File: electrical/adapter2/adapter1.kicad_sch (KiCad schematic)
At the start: 7 parts, among them J2 Conn_01x08_Pin

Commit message: start working on adapter2 PCB
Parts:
- added C1, C10, C11, C12, C2, C5, C7, C8, C9: 105, Capacitor_SMD:C_0805_2012Metric_Pad1.18x1.45mm_HandSolder, symbol Device:C
- added C15, C3: 104 !, Capacitor_SMD:C_0805_2012Metric_Pad1.18x1.45mm_HandSolder, symbol Device:C
- added C4, C6: 4.7uF/50V, Capacitor_SMD:C_0805_2012Metric_Pad1.18x1.45mm_HandSolder, symbol Device:C
- added D1, D2, D3: MBR0530, Diode_SMD:D_SOD-123, symbol Diode:MBR0530
- added J3, J4: 0.5 mm, 24P, Connector_FFC-FPC:Jushuo_AFC07-S24FCA-00_1x24-1MP_P0.50_Horizontal, symbol Connector_Generic_MountingPin:Conn_01x24_MountingPin
- added JP3: SolderJumper_3_Bridged12, Jumper:SolderJumper-3_P1.3mm_Bridged12_RoundedPad1.0x1.5mm, symbol Jumper:SolderJumper_3_Bridged12
- added JP4: SolderJumper_2_Open, Jumper:SolderJumper-2_P1.3mm_Open_TrianglePad1.0x1.5mm, symbol Jumper:SolderJumper_2_Open
- added L1: 68uH, symbol Device:L
- added Q1: BSS138, Package_TO_SOT_SMD:SOT-23, symbol Transistor_FET:BSS138
- added Q2: AO3401A, Package_TO_SOT_SMD:SOT-23, symbol Transistor_FET:AO3401A
- added Q3: S8050 SMD, Package_TO_SOT_SMD:SOT-23, symbol Transistor_BJT:BC817
- added R1: 0.47R, Resistor_SMD:R_0805_2012Metric_Pad1.20x1.40mm_HandSolder, symbol Device:R
- added R2, R5: 10k, Resistor_SMD:R_0805_2012Metric_Pad1.20x1.40mm_HandSolder, symbol Device:R
- added R3: 100k, Resistor_SMD:R_0805_2012Metric_Pad1.20x1.40mm_HandSolder, symbol Device:R
- added R6: 1k, Resistor_SMD:R_0805_2012Metric_Pad1.20x1.40mm_HandSolder, symbol Device:R
- added R7, R8: 47k, Resistor_SMD:R_0805_2012Metric_Pad1.20x1.40mm_HandSolder, symbol Device:R
- added U1: ~, fw16_epaper:RP2040-Tiny, symbol fw16_epaper:RP2040-Tiny
- renumbered R1 to R10
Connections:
- net +3V3: now also C15.2, C4.2, JP4.1 (A), L1.1, Q2.2 (S), R3.2
- net GND: now also C1.1, C10.1, C11.1, C12.1, C15.1, C2.1, C3.1, C4.1, C5.1, C7.1, C8.1, C9.1, D1.1 (K), J3.8 (Pin_8), J3.MP (MountPin), J4.17 (Pin_17), JP3.1 (A), Q3.2 (E), R1.1, R2.1, R7.1, R8.1, U1.21 (GND)
- net SLEEP: now also U1.0
- new net: Q3.1 (B), R5.1, R7.2
- new net: C12.2, J3.1 (Pin_1), J4.24 (Pin_24)
- new net: J3.18 (Pin_18), J4.7 (Pin_7)
- new net: J3.19 (Pin_19), J4.6 (Pin_6)
- new net: C2.2, J3.20 (Pin_20), J4.5 (Pin_5)
- new net: C1.2, J3.21 (Pin_21), J4.4 (Pin_4)
- new net: J3.24 (Pin_24), J4.1 (Pin_1)
- new net: C10.2, J3.3 (Pin_3), J4.22 (Pin_22)
- new net: C8.2, J3.5 (Pin_5), J4.20 (Pin_20)
- new net: C7.2, J3.6 (Pin_6), J4.19 (Pin_19)
- new net: C5.2, J3.7 (Pin_7), J4.18 (Pin_18)
- new net: C6.2, D3.2 (A), L1.2, Q1.3 (D)
- new net: Q1.1 (G), R2.2
- new net: Q2.1 (G), Q3.3 (C), R3.1
- new net: Q1.2 (S), R1.2
- new net: C6.1, D1.2 (A), D2.1 (K)
- new net 3V3_EP: C3.2, J3.10 (Pin_10), J3.9 (Pin_9), J4.15 (Pin_15), J4.16 (Pin_16), JP3.3 (B), Q2.3 (D)
- new net 3V3_RPI: JP4.2 (B), U1.20 (3V3)
- new net 5V_RPI: U1.22 (5V)
- new net BS: J3.17 (Pin_17), J4.8 (Pin_8), JP3.2 (C)
- new net BUSY: J3.16 (Pin_16), J4.9 (Pin_9), U1.14
- new net CS: J3.13 (Pin_13), J4.12 (Pin_12), U1.19 (29)
- new net DC: J3.14 (Pin_14), J4.11 (Pin_11), U1.18 (28)
- new net DIN: J3.11 (Pin_11), J4.14 (Pin_14), U1.17 (27)
- new net GDR: J3.23 (Pin_23), J4.2 (Pin_2)
- new net PREVGH: C9.2, D3.1 (K), J3.4 (Pin_4), J4.21 (Pin_21)
- new net PREVGL: C11.2, D2.2 (A), J3.2 (Pin_2), J4.23 (Pin_23)
- new net RESE: J3.22 (Pin_22), J4.3 (Pin_3)
- new net RST: J3.15 (Pin_15), J4.10 (Pin_10), R5.2, R6.1, U1.15
- new net SCK: J3.12 (Pin_12), J4.13 (Pin_13), U1.16 (26)
- new net VCC_EN: R6.2, R8.2
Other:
- note added: "ADC"
- note added: "This is a mirrored connector on top. It could be used to solder the FPC directly (without socket) but that's probably not a good idea ;-)"
- note added: "This is pin 1. Connector is flipped in KiCad."
- note added: "see https://files.waveshare.com/upload/1/1c/Pico-ePaper-3.7.pdf"

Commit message: adapter2: routing done and DRC clean
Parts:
- removed R6: 1k, Resistor_SMD:R_0805_2012Metric_Pad1.20x1.40mm_HandSolder, symbol Device:R
- removed R8: 47k, Resistor_SMD:R_0805_2012Metric_Pad1.20x1.40mm_HandSolder, symbol Device:R
- added J5: ~, fw16_epaper:TouchConnector, symbol Connector:Conn_01x04_Socket
- L1: footprint (none) -> Inductor_SMD:L_Bourns-SRN4018
- R10: footprint Resistor_SMD:R_0603_1608Metric_Pad0.98x0.95mm_HandSolder -> Resistor_SMD:R_0805_2012Metric_Pad1.20x1.40mm_HandSolder
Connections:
- net +3V3: no longer C4.2, L1.1
- net 3V3_EP: now also C4.2, L1.1
- net BUSY: now also U1.5; no longer U1.14
- net CS: now also U1.8; no longer U1.19 (29)
- net DC: now also U1.7; no longer U1.18 (28)
- net DIN: now also U1.10; no longer U1.17 (27)
- net GDR: now also Q1.1 (G), R2.2
- net GND: now also J4.MP (MountPin)
- net RESE: now also Q1.2 (S), R1.2
- net RST: now also U1.6; no longer U1.15
- net SCK: now also U1.9; no longer U1.16 (26)
- net at U1.1: now also U1.19 (29), J5.1 (Pin_1)
- net at U1.2: now also U1.18 (28), J5.2 (Pin_2)
- net at U1.3: now also U1.17 (27), J5.3 (Pin_3)
- net at U1.4: now also U1.16 (26), J5.4 (Pin_4)
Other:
- note added: "Touch"

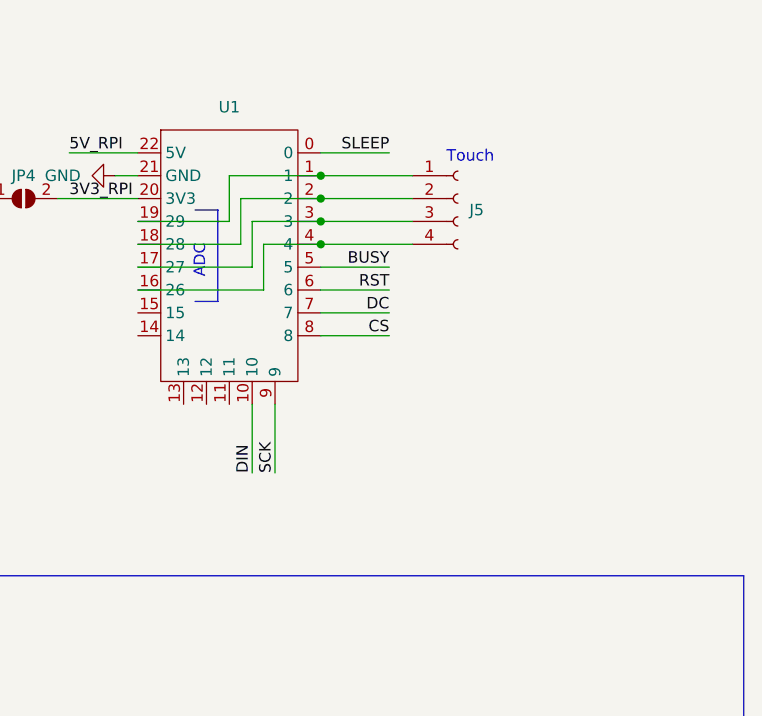
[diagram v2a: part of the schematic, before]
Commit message: add ATECC608
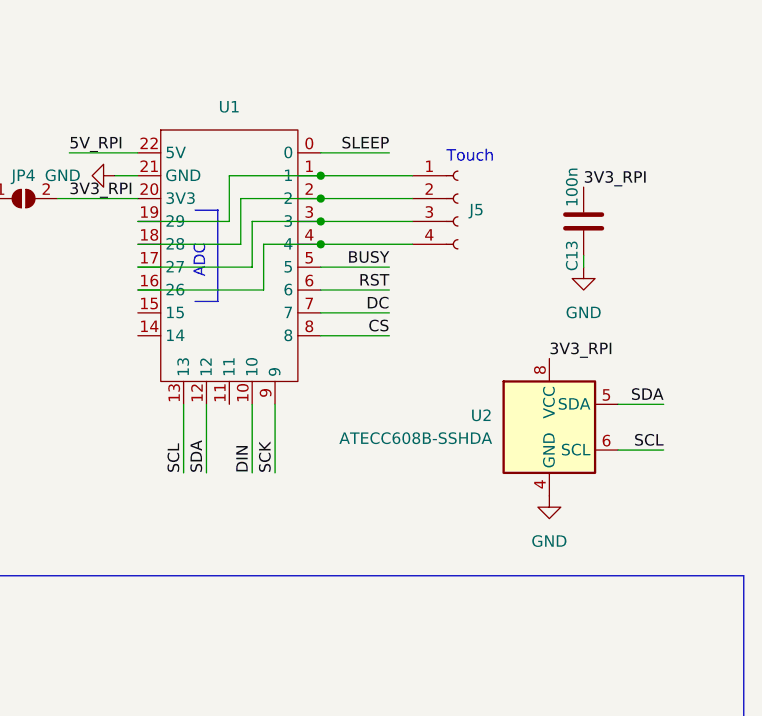
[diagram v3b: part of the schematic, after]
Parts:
- added C13: 100n, Capacitor_SMD:C_0805_2012Metric_Pad1.18x1.45mm_HandSolder, symbol Device:C
- added U2: ATECC608B-SSHDA, Package_SO:SOIC-8_3.9x4.9mm_P1.27mm, symbol Security:ATECC608B-SSHDA
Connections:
- net 3V3_RPI: now also C13.2, U2.8 (VCC)
- net GND: now also C13.1, U2.4 (GND)
- net SDA: now reaches U1.12
- net SDA: now also U2.5 (SDA)
- net SCL: now reaches U1.13
- net SCL: now also U2.6 (SCL)
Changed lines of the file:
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@@
+    (stroke (width 0) (type default))
+  )
+  (wire (pts (xy 173.99 59.69) (xy 179.07 59.69))
     (stroke (width 0) (type default))
   )
@@
     (stroke (width 0) (type default))
   )
+  (wire (pts (xy 128.27 59.69) (xy 128.27 67.31))
+    (stroke (width 0) (type default))
+  )
+  (wire (pts (xy 170.18 44.45) (xy 170.18 43.18))
+    (stroke (width 0) (type default))
+  )
   (wire (pts (xy 22.86 40.64) (xy 30.48 40.64))
     (stroke (width 0) (type default))
@@
     (stroke (width 0) (type default))
   )
+  (wire (pts (xy 173.99 64.77) (xy 179.07 64.77))
+    (stroke (width 0) (type default))
+  )
   (wire (pts (xy 148.59 49.53) (xy 140.97 49.53))
     (stroke (width 0) (type default))
@@
   )
   (wire (pts (xy 53.34 40.64) (xy 60.96 40.64))
+    (stroke (width 0) (type default))
+  )
+  (wire (pts (xy 125.73 59.69) (xy 125.73 67.31))
     (stroke (width 0) (type default))
   )
@@
     (effects (font (size 1.27 1.27)) (justify left bottom))
   )
+  (label "3V3_RPI" (at 170.18 35.56 0) (fields_autoplaced)
+    (effects (font (size 1.27 1.27)) (justify left bottom))
+  )
   (label "GDR" (at 44.45 97.79 0) (fields_autoplaced)
+    (effects (font (size 1.27 1.27)) (justify left bottom))
+  )
+  (label "SCL" (at 125.73 67.31 90) (fields_autoplaced)
     (effects (font (size 1.27 1.27)) (justify left bottom))
   )
@@
     (effects (font (size 1.27 1.27)) (justify left bottom))
   )
+  (label "3V3_RPI" (at 166.37 54.61 0) (fields_autoplaced)
+    (effects (font (size 1.27 1.27)) (justify left bottom))
+  )
   (label "RST" (at 44.45 118.11 0) (fields_autoplaced)
     (effects (font (size 1.27 1.27)) (justify left bottom))
@@
   (label "BS" (at 44.45 113.03 0) (fields_autoplaced)
     (effects (font (size 1.27 1.27)) (justify left bottom))
+  )
+  (label "SCL" (at 179.07 64.77 180) (fields_autoplaced)
+    (effects (font (size 1.27 1.27)) (justify right bottom))
   )
   (label "RESE" (at 44.45 100.33 0) (fields_autoplaced)
@@
     (effects (font (size 1.27 1.27)) (justify right bottom))
   )
+  (label "SDA" (at 128.27 67.31 90) (fields_autoplaced)
+    (effects (font (size 1.27 1.27)) (justify left bottom))
+  )
   (label "RUN" (at 62.23 54.61 0) (fields_autoplaced)
     (effects (font (size 1.27 1.27)) (justify left bottom))
@@
   (label "RUN" (at 38.1 64.77 90) (fields_autoplaced)
     (effects (font (size 1.27 1.27)) (justify left bottom))
+  )
+  (label "SDA" (at 179.07 59.69 180) (fields_autoplaced)
+    (effects (font (size 1.27 1.27)) (justify right bottom))
   )
   (label "PREVGL" (at 111.76 191.77 0) (fields_autoplaced)
@@
         (path "/a61be344-1595-4e77-a084-104edbf00aaf"
           (reference "#PWR014") (unit 1)
+        )
+      )
+    )
+  )
+  (symbol (lib_id "power:GND") (at 166.37 69.85 0) (unit 1)
+    (in_bom yes) (on_board yes) (dnp no) (fields_autoplaced)
+    (property "Reference" "#PWR036" (at 166.37 76.2 0)
+      (effects (font (size 1.27 1.27)) hide)
+    )
+    (property "Value" "GND" (at 166.37 74.93 0)
+      (effects (font (size 1.27 1.27)))
+    )
+    (property "Footprint" "" (at 166.37 69.85 0)
+      (effects (font (size 1.27 1.27)) hide)
+    )
+    (property "Datasheet" "" (at 166.37 69.85 0)
+      (effects (font (size 1.27 1.27)) hide)
+    )
+    (pin "1")
+    (instances
+      (project "adapter1"
+        (path "/a61be344-1595-4e77-a084-104edbf00aaf"
+          (reference "#PWR036") (unit 1)
         )
       )
@@
     )
   )
+  (symbol (lib_id "Device:C") (at 170.18 39.37 180) (unit 1)
+    (in_bom yes) (on_board yes) (dnp no)
+    (property "Reference" "C13" (at 168.91 43.18 90)
+      (effects (font (size 1.27 1.27)))
+    )
+    (property "Value" "100n" (at 168.91 35.56 90)
+      (effects (font (size 1.27 1.27)))
+    )
+    (property "Footprint" "Capacitor_SMD:C_0805_2012Metric_Pad1.18x1.45mm_HandSolder" (at 169.2148 35.56 0)
+      (effects (font (size 1.27 1.27)) hide)
+    )
+    (property "Datasheet" "~" (at 170.18 39.37 0)
+      (effects (font (size 1.27 1.27)) hide)
+    )
+    (pin "2")
+    (pin "1")
+    (instances
+      (project "adapter1"
+        (path "/a61be344-1595-4e77-a084-104edbf00aaf"
+          (reference "C13") (unit 1)
+        )
+      )
+    )
+  )
   (symbol (lib_id "power:+3V3") (at 63.5 74.93 90) (unit 1)
     (in_bom yes) (on_board yes) (dnp no) (fields_autoplaced)
@@
         (path "/a61be344-1595-4e77-a084-104edbf00aaf"
           (reference "JP4") (unit 1)
+        )
+      )
+    )
+  )
+  (symbol (lib_id "Security:ATECC608B-SSHDA") (at 166.37 62.23 0) (unit 1)
+    (in_bom yes) (on_board yes) (dnp no) (fields_autoplaced)
+    (property "Reference" "U2" (at 160.02 60.96 0)
+      (effects (font (size 1.27 1.27)) (justify right))
+    )
+    (property "Value" "ATECC608B-SSHDA" (at 160.02 63.5 0)
+      (effects (font (size 1.27 1.27)) (justify right))
+    )
+    (property "Footprint" "Package_SO:SOIC-8_3.9x4.9mm_P1.27mm" (at 166.37 62.23 0)
+      (effects (font (size 1.27 1.27)) hide)
+    )
+    (property "Datasheet" "https://ww1.microchip.com/downloads/aemDocuments/documents/SCBU/ProductDocuments/DataSheets/ATECC608B-CryptoAuthentication-Device-Summary-Data-Sheet-DS40002239B.pdf" (at 170.18 55.88 0)
+      (effects (font (size 1.27 1.27)) hide)
+    )
+    (pin "5")
+    (pin "6")
+    (pin "3")
+    (pin "4")
+    (pin "1")
+    (pin "2")
+    (pin "8")
+    (pin "7")
+    (instances
+      (project "adapter1"
+        (path "/a61be344-1595-4e77-a084-104edbf00aaf"
+          (reference "U2") (unit 1)
         )
       )
@@
         )
       )
+    )
+  )
+  (symbol (lib_id "power:GND") (at 170.18 44.45 0) (unit 1)
+    (in_bom yes) (on_board yes) (dnp no) (fields_autoplaced)
+    (property "Reference" "#PWR037" (at 170.18 50.8 0)
+      (effects (font (size 1.27 1.27)) hide)
+    )
+    (property "Value" "GND" (at 170.18 49.53 0)
+      (effects (font (size 1.27 1.27)))
+    )
+    (property "Footprint" "" (at 170.18 44.45 0)
+      (effects (font (size 1.27 1.27)) hide)
+    )
+    (property "Datasheet" "" (at 170.18 44.45 0)
+      (effects (font (size 1.27 1.27)) hide)
+    )
+    (pin "1")
+    (instances
+      (project "adapter1"
+        (path "/a61be344-1595-4e77-a084-104edbf00aaf"
+          (reference "#PWR037") (unit 1)
+        )
+      )

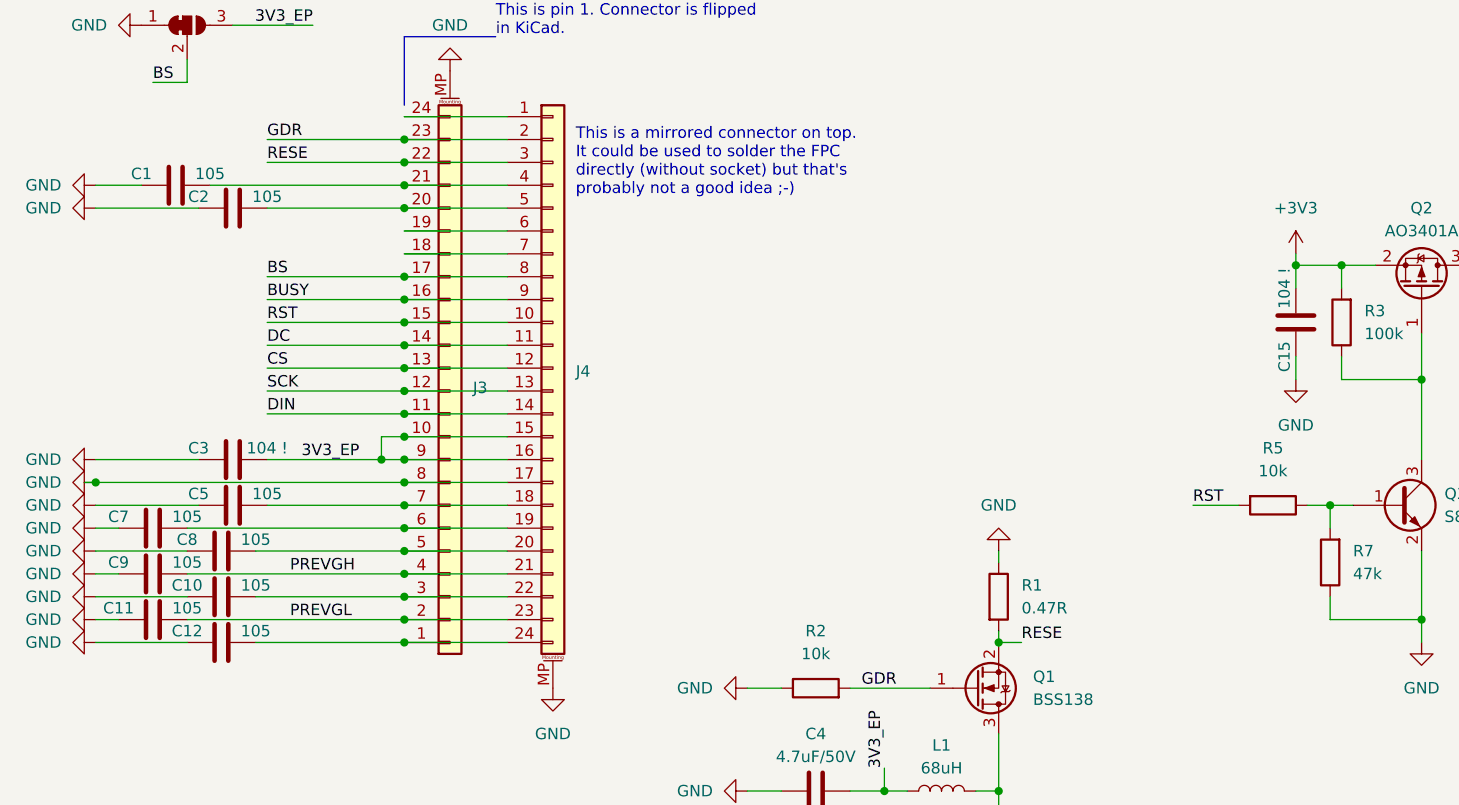
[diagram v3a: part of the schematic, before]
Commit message: add LCSC part numbers
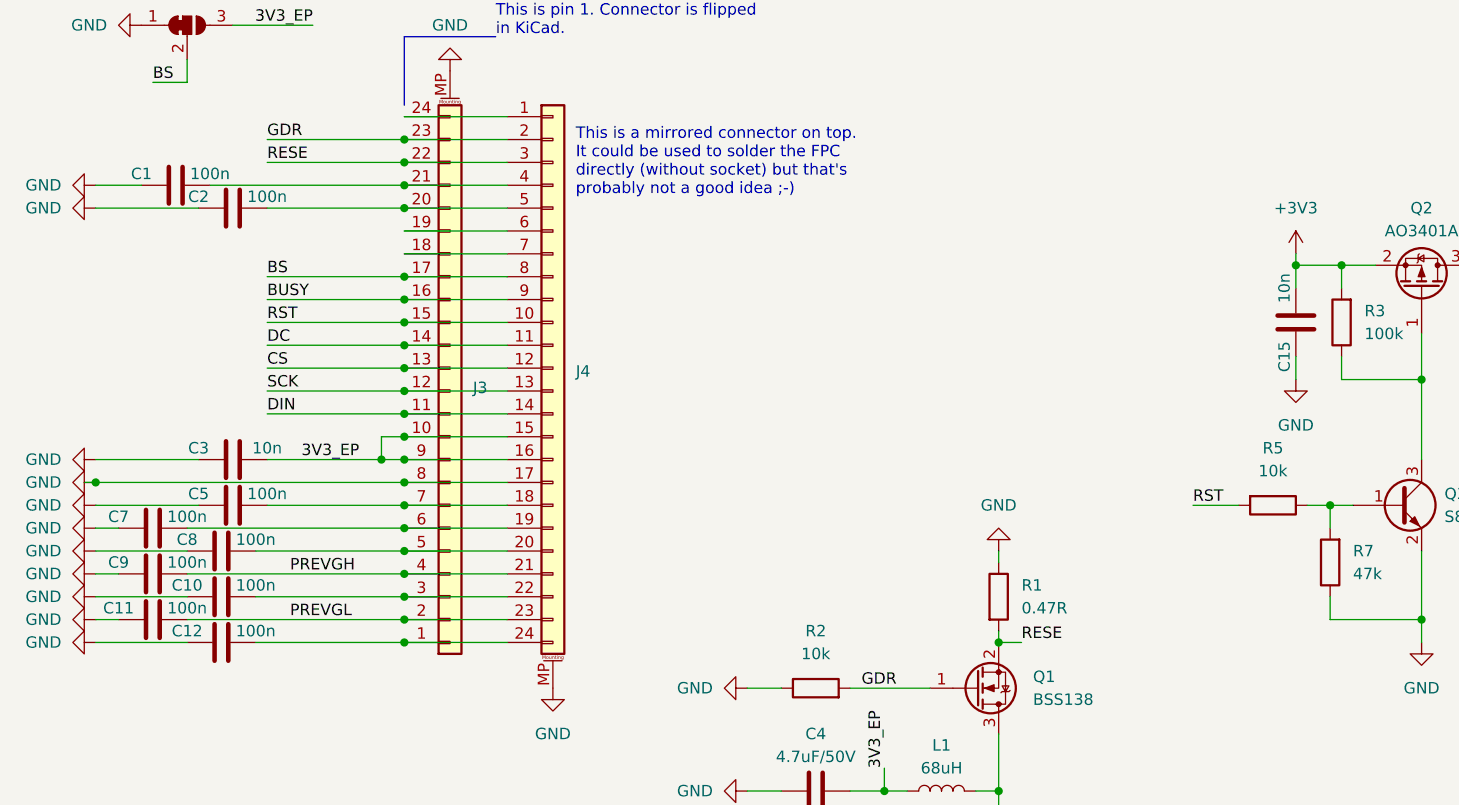
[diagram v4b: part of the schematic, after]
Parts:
- C1, C10, C11, C12, C2, C5, C7, C8, C9: value 105 -> 100n; LCSC (none) -> C720961
- C13: LCSC (none) -> C720961
- C15, C3: value 104 ! -> 10n; LCSC (none) -> C282728
- C4, C6: LCSC (none) -> C513770
- D1, D2, D3: LCSC (none) -> C475718
- J1, J2, J5, R10, TP1, TP2: now left out of the parts list
- J3: LCSC (none) -> C11092
- J4: LCSC (none) -> C11092; now left out of the parts list
- L1: LCSC (none) -> C241167
- Q1: LCSC (none) -> C5224264
- Q2: LCSC (none) -> C347476
- Q3: LCSC (none) -> C5184427
- R1: LCSC (none) -> C25040
- R2, R5: LCSC (none) -> C2930231
- R3: LCSC (none) -> C3017875
- R7: LCSC (none) -> C104351
- U2: LCSC (none) -> C1518769
